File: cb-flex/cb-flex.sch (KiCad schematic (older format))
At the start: 26 parts, among them P3 CONN_01X01, SW1 SW_PUSH_SMALL, U1 SI7021, U4 ANTENNA

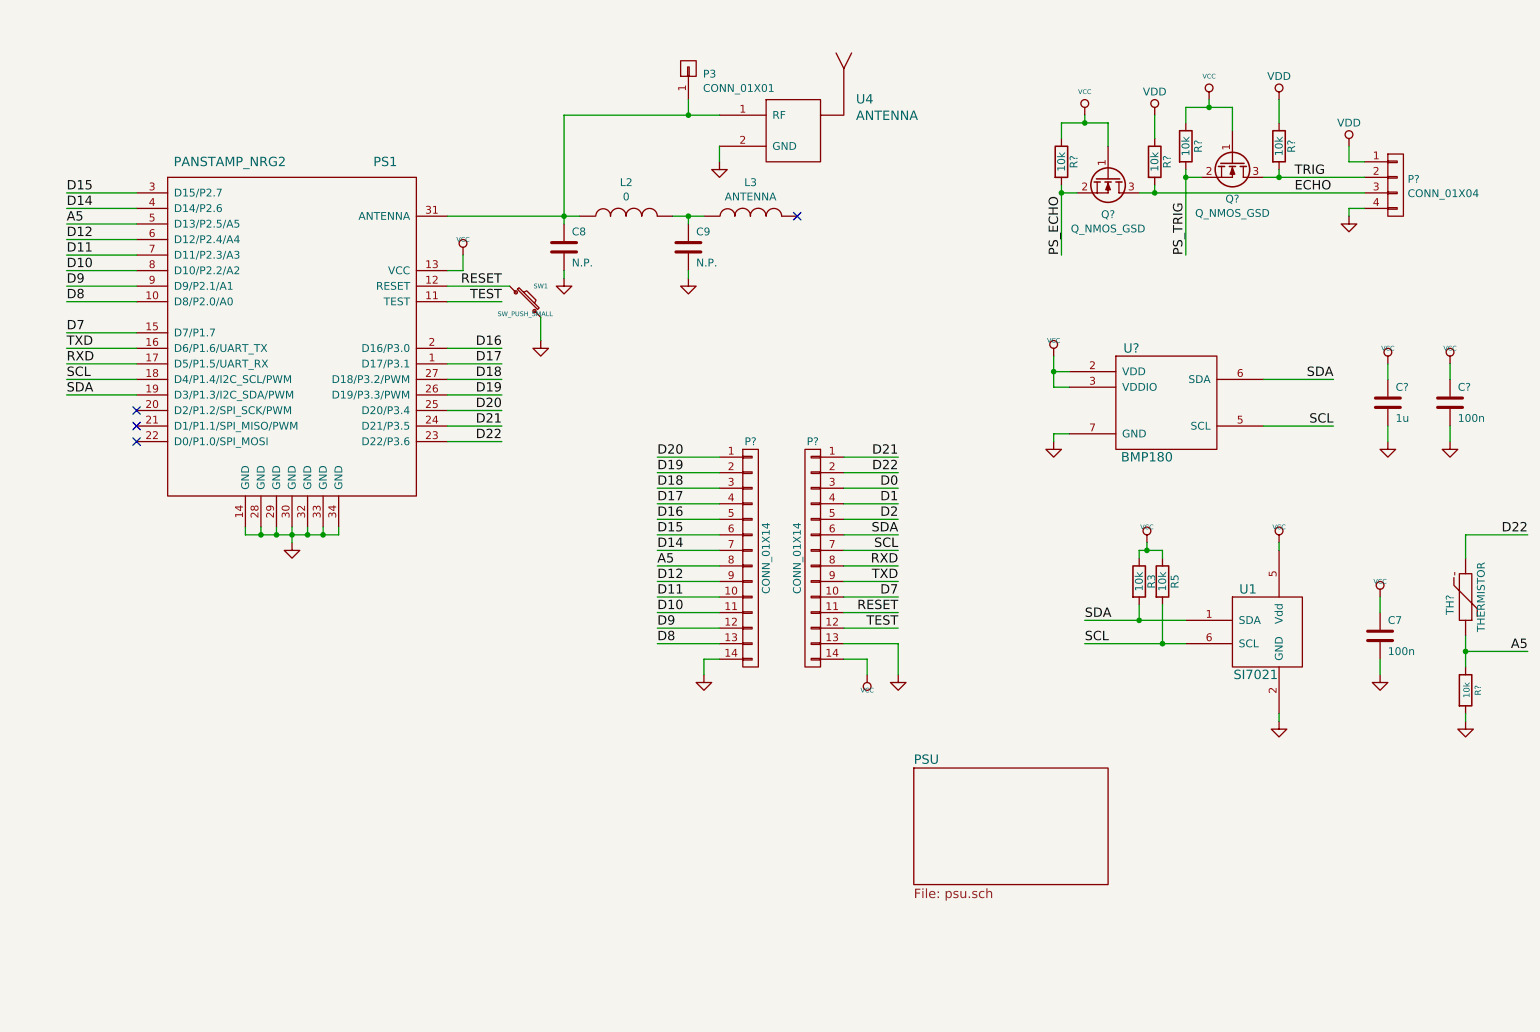
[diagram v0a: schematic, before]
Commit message: Finishing schematic and starting PCB layout
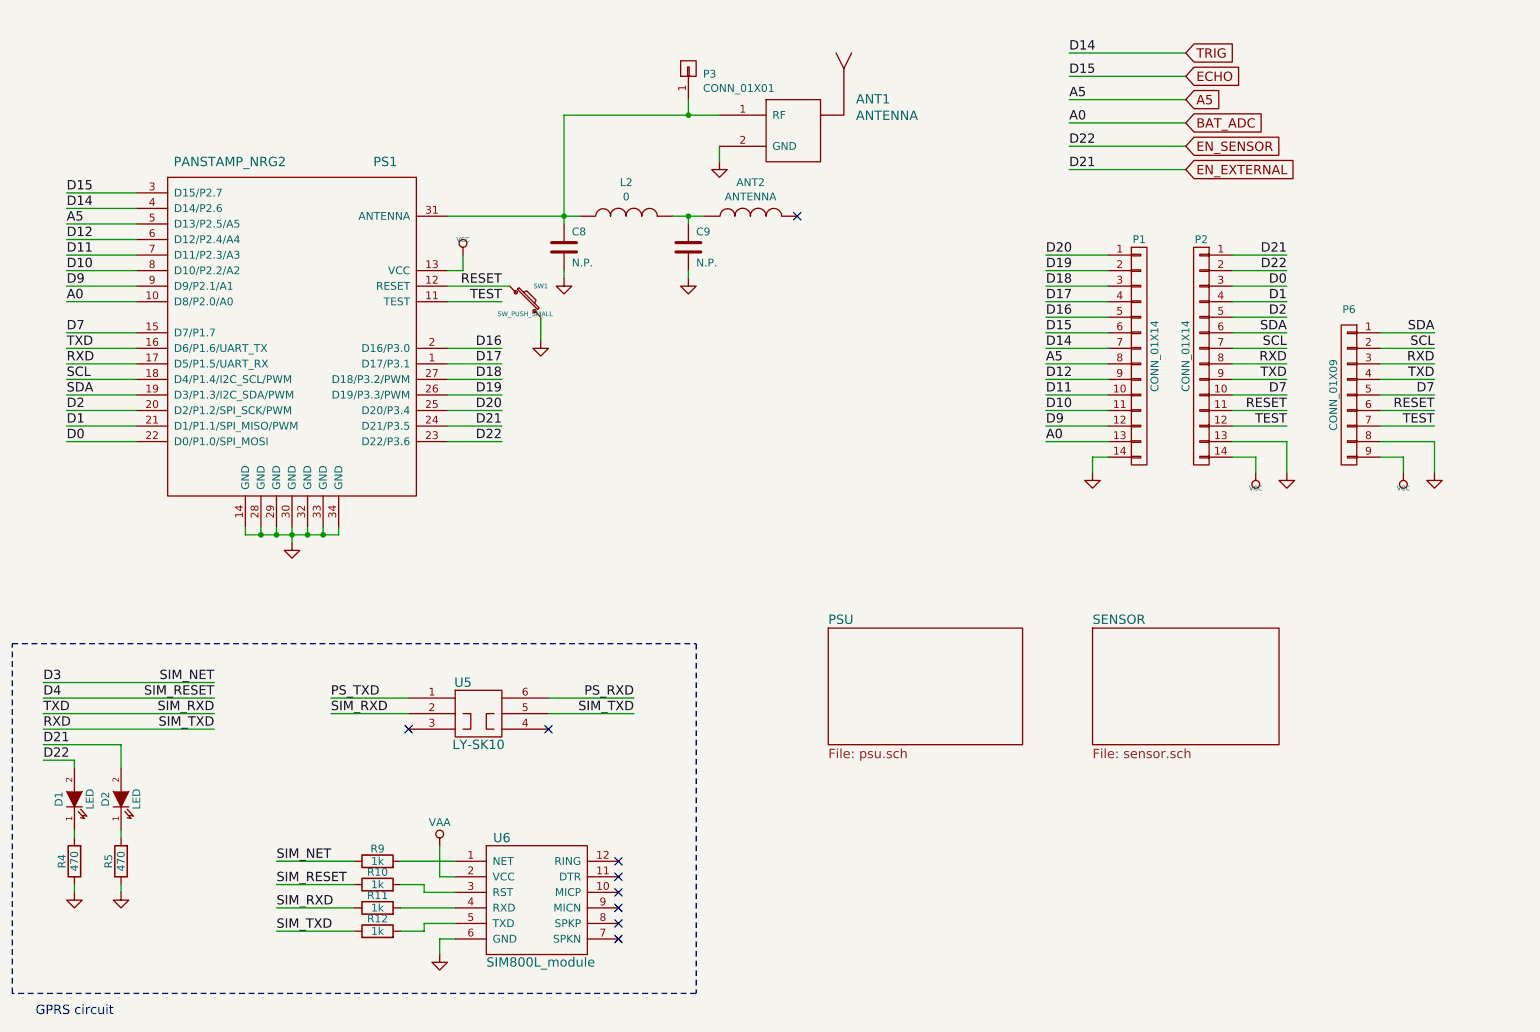
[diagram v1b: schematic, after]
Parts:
- removed C7, C?: 100n, mysmd:SM0603S, symbol C
- removed C?: 1u, mysmd:SM0603S, symbol C
- removed P?: CONN_01X04, symbol CONN_01X04
- removed Q? (x2): Q_NMOS_GSD, mysmd:SOT23, symbol Q_NMOS_GSD
- removed R3, R? (x5): 10k, mysmd:SM0603S, symbol R
- removed TH?: THERMISTOR, mysmd:SM0603S, symbol THERMISTOR
- removed U1: SI7021, mysmd:DFN-6, symbol SI7021
- removed U?: BMP180, mysmd:BMP180, symbol BMP180
- added D1, D2: LED, mysmd:SM0603S_POL, symbol LED
- added P6: CONN_01X09, Pin_Headers:Pin_Header_Straight_1x09, symbol CONN_01X09
- added R10, R11, R12, R9: 1k, mysmd:SM0603S, symbol R
- added R4: 470, mysmd:SM0603S, symbol R
- added U5: LY-SK10, mysmd:LY-SK10, symbol LY-SK10
- added U6: SIM800L_module, mymods:SIM800L_MODULE, symbol SIM800L_module
- R5: value 10k -> 470
- gave numbers to parts that had none: 2
- renumbered U4 to ANT1, L3 to ANT2
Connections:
- net D14 is gone; now on net TRIG: P1.7 (P7), PS1.4 (D14/P2.6)
- net D15 is gone; now on net ECHO: P1.6 (P6), PS1.3 (D15/P2.7)
- net D0: now also PS1.22 (D0/P1.0/SPI_MOSI)
- net D1: now also PS1.21 (D1/P1.1/SPI_MISO/PWM)
- net D2: now also PS1.20 (D2/P1.2/SPI_SCK/PWM)
- net D7: now also P6.5 (P5)
- net GND: now also R5.1, P6.8 (P8), R4.1, U6.6 (GND)
- net RESET: now also P6.6 (P6)
- net RXD: now also P6.3 (P3), R12.1, U5.5
- net SCL: now also P6.2 (P2); no longer R5.2
- net SDA: now also P6.1 (P1)
- net TEST: now also P6.7 (P7)
- net VCC: now also P6.9 (P9); no longer R5.1
- net D21 renamed EN_EXTERNAL
- net EN_EXTERNAL: now also D2.2 (A)
- net D22 renamed EN_SENSOR
- net EN_SENSOR: now also D1.2 (A)
- net D8 renamed BAT_ADC
- net TXD renamed SIM_RXD
- net SIM_RXD: now also P6.4 (P4), R11.1, U5.2
- new net: D2.1 (K), R5.2
- new net: R9.2, U6.1 (NET)
- new net: R10.2, U6.3 (RST)
- new net: R11.2, U6.4 (RXD)
- new net: R12.2, U6.5 (TXD)
- new net: D1.1 (K), R4.2
- new net D3: R9.1
- new net D4: R10.1
- new net PS_RXD: U5.6
- new net PS_TXD: U5.1
- new net VAA: U6.2 (VCC)
- no-connect marks 4 -> 9
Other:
- note added: "GPRS circuit"
- moved on the sheet: P1, P2

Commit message: Finishing layout
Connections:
- net D16 is gone; now on net EN_EXTERNAL: P1.5 (P5), PS1.2 (D16/P3.0)
- net D20 is gone; now on net EN_SENSOR: P1.1 (P1), PS1.25 (D20/P3.4)
- net D3 is gone; now on net ACC_INT1: R9.1
- net D4 is gone; now on net ACC_INT2: R10.1
- net PS_RXD is gone; now on net RXD: U5.6
- net EN_EXTERNAL: no longer D2.2 (A), P2.1 (P1), PS1.24 (D21/P3.5)
- net EN_SENSOR: no longer D1.2 (A), P2.2 (P2), PS1.23 (D22/P3.6)
- net RXD: no longer R12.1, U5.5
- net SIM_RXD: no longer P2.9 (P9), P6.4 (P4), PS1.16 (D6/P1.6/UART_TX)
- net BAT_ADC renamed +BATT
- net D0 renamed EN_ACC
- net D1 renamed ACC_INT1
- net D2 renamed ACC_INT2
- net PS_TXD renamed TXD
- net TXD: now also P2.9 (P9), P6.4 (P4), PS1.16 (D6/P1.6/UART_TX)
- new net D21: D2.2 (A), P2.1 (P1), PS1.24 (D21/P3.5)
- new net D22: D1.2 (A), P2.2 (P2), PS1.23 (D22/P3.6)
- new net SIM_TXD: R12.1, U5.5
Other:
- moved on the sheet: P1, P2, P6

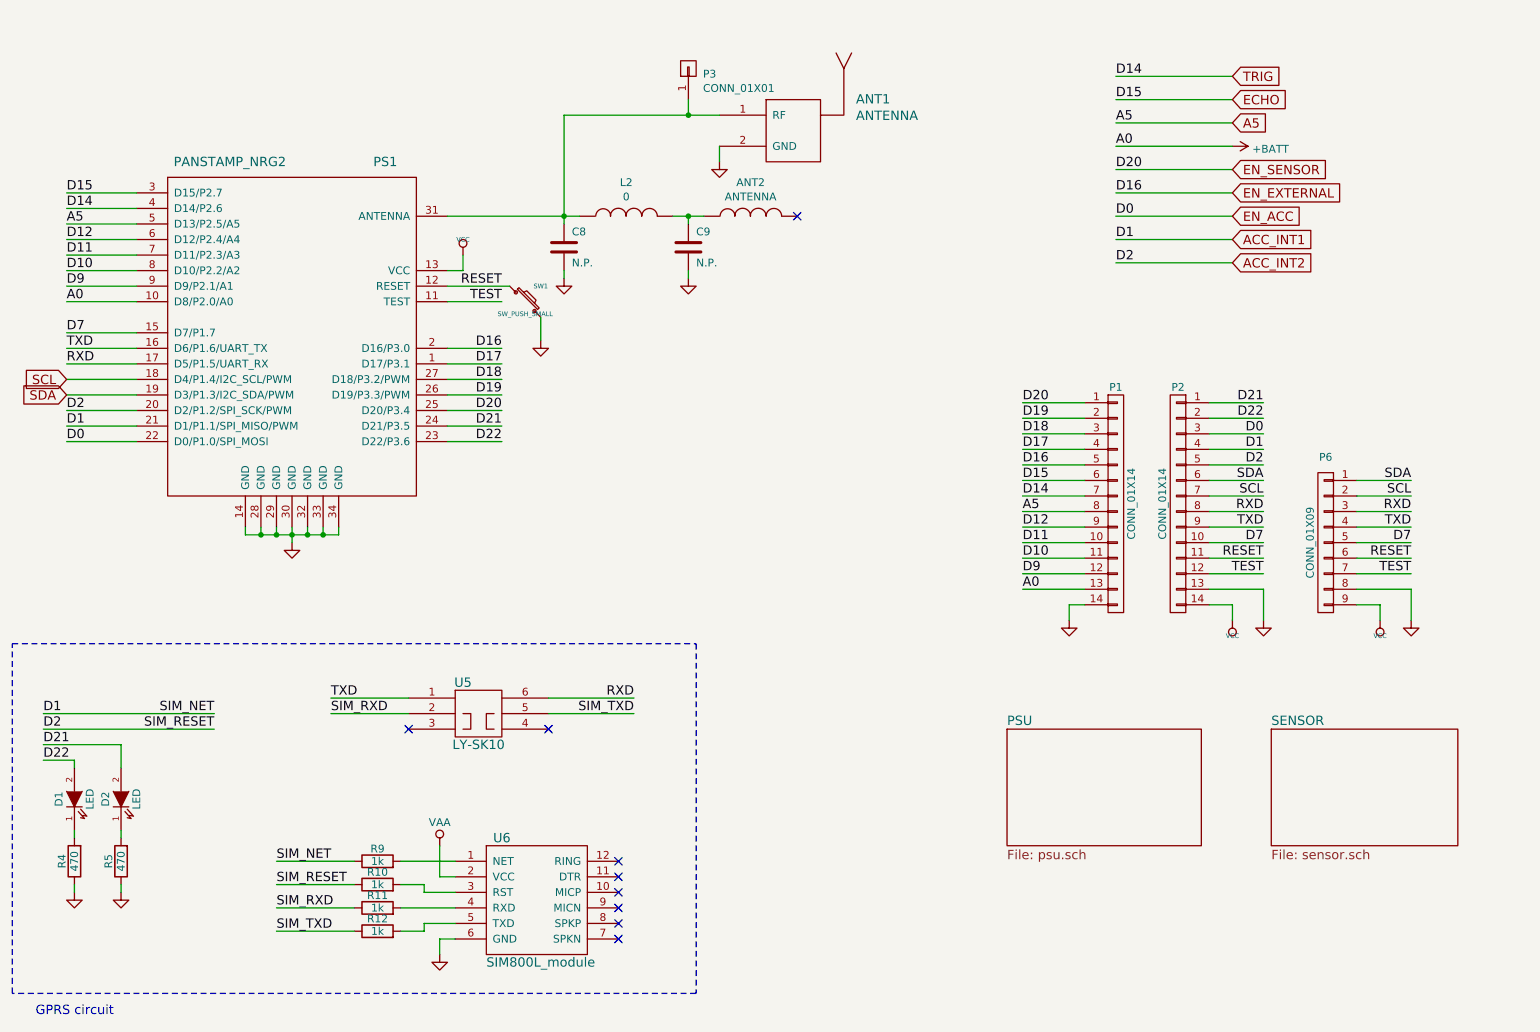
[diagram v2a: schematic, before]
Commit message: PCB layour finished
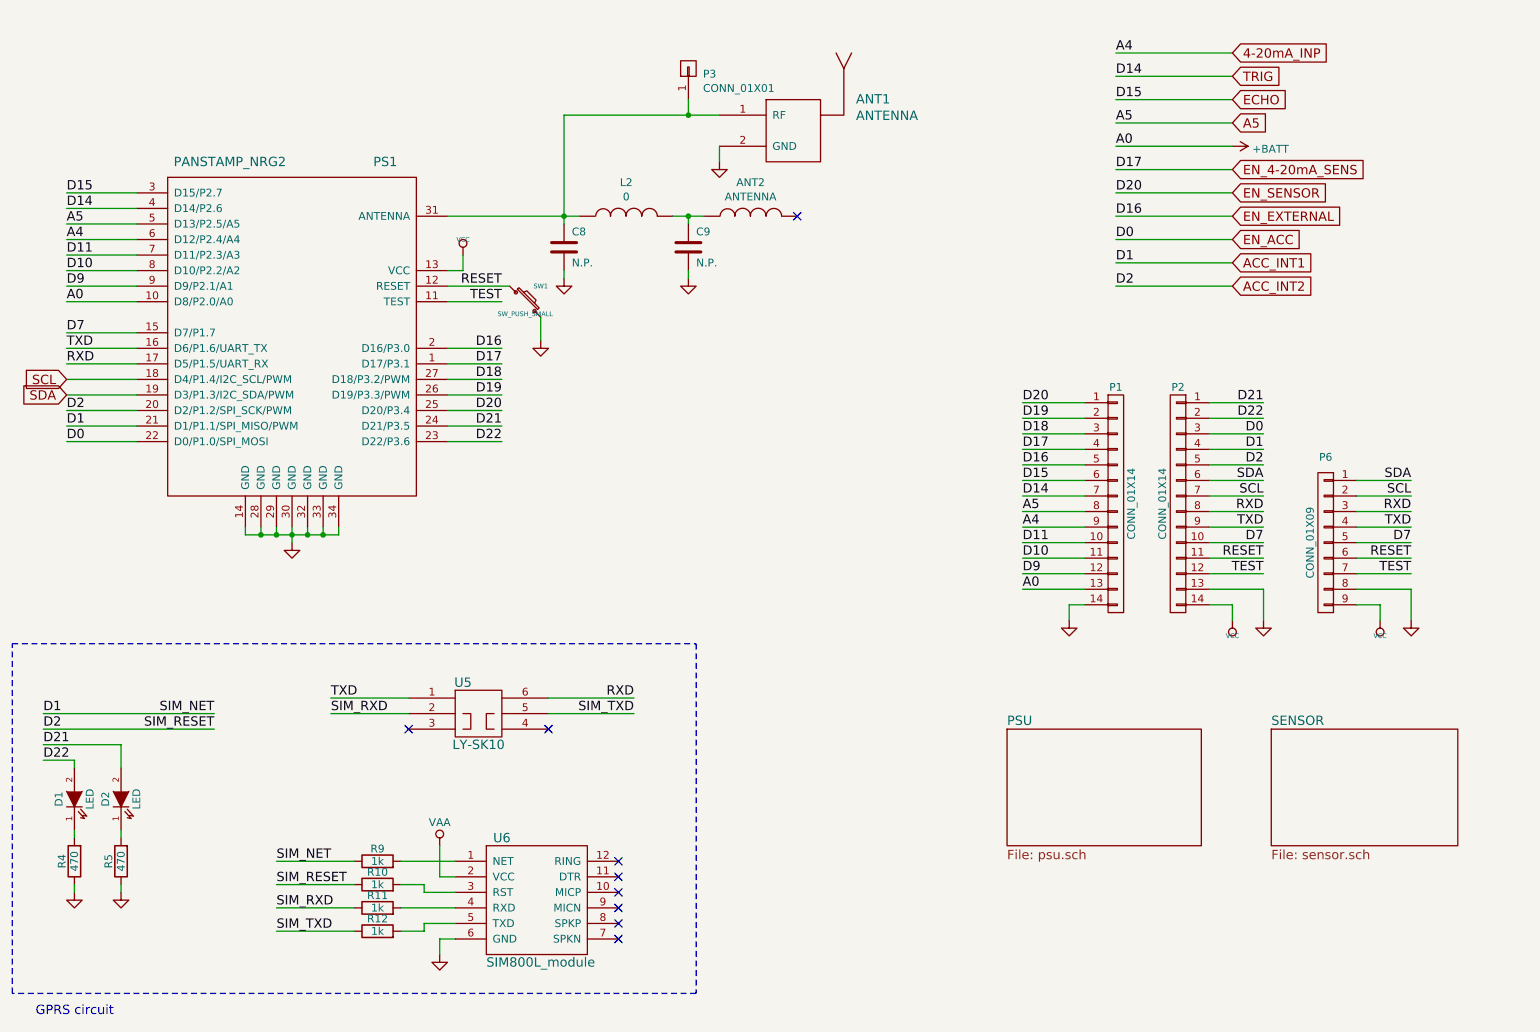
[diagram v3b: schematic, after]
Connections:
- net D12 renamed 4-20mA_INP
- net D17 renamed EN_4-20mA_SENS
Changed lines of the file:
@@
 D11
 Text Label 1500 2100 0    60   ~ 0
-D12
+A4
 Text Label 1500 1900 0    60   ~ 0
 D14
@@
 A5
 Text Label 7650 3950 0    60   ~ 0
-D12
+A4
 Text Label 7650 4050 0    60   ~ 0
 D11
@@
 Text Label 1500 2000 0    60   ~ 0
 A5
-Text GLabel 9000 1650 2    60   Input ~ 0
+Text GLabel 9000 1800 2    60   Input ~ 0
 EN_SENSOR
 Wire Wire Line
-	9000 1650 8250 1650
-Text Label 8250 1650 0    60   ~ 0
+	9000 1800 8250 1800
+Text Label 8250 1800 0    60   ~ 0
 D20
 Text GLabel 9000 1350 2    60   Input ~ 0
@@
 Text Label 8250 1200 0    60   ~ 0
 D15
-Text GLabel 9000 1800 2    60   Input ~ 0
+Text GLabel 9000 1950 2    60   Input ~ 0
 EN_EXTERNAL
 Wire Wire Line
-	9000 1800 8250 1800
-Text Label 8250 1800 0    60   ~ 0
+	9000 1950 8250 1950
+Text Label 8250 1950 0    60   ~ 0
 D16
 $Comp
@@
 Text Label 8250 1500 0    60   ~ 0
 A0
+Text GLabel 9000 2250 2    60   Input ~ 0
+ACC_INT1
+Wire Wire Line
+	9000 2250 8250 2250
+Text Label 8250 2250 0    60   ~ 0
+D1
+Text GLabel 9000 2400 2    60   Input ~ 0
+ACC_INT2
+Wire Wire Line
+	9000 2400 8250 2400
+Text Label 8250 2400 0    60   ~ 0
+D2
 Text GLabel 9000 2100 2    60   Input ~ 0
-ACC_INT1
+EN_ACC
 Wire Wire Line
 	9000 2100 8250 2100
 Text Label 8250 2100 0    60   ~ 0
-D1
-Text GLabel 9000 2250 2    60   Input ~ 0
-ACC_INT2
-Wire Wire Line
-	9000 2250 8250 2250
-Text Label 8250 2250 0    60   ~ 0
-D2
-Text GLabel 9000 1950 2    60   Input ~ 0
-EN_ACC
-Wire Wire Line
-	9000 1950 8250 1950
-Text Label 8250 1950 0    60   ~ 0
 D0
 Text GLabel 1500 3000 0    60   Input ~ 0
@@
 SDA
 $Comp
-L +BATT #PWR?
+L +BATT #PWR016
 U 1 1 56C22796
 P 9000 1500
-F 0 "#PWR?" H 9000 1350 50  0001 C CNN
+F 0 "#PWR016" H 9000 1350 50  0001 C CNN
 F 1 "+BATT" V 9018 1628 50  0000 L CNN
 F 2 "" H 9000 1500 50  0000 C CNN
@@
 	0    1    1    0
 $EndComp
+Text Label 8250 900  0    60   ~ 0
+A4
+Text GLabel 9000 900  2    60   Input ~ 0
+4-20mA_INP
+Wire Wire Line
+	9000 900  8250 900
+Text GLabel 9000 1650 2    60   Input ~ 0
+EN_4-20mA_SENS
+Wire Wire Line
+	9000 1650 8250 1650
+Text Label 8250 1650 0    60   ~ 0
+D17
 $EndSCHEMATC

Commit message: PCB layout finished
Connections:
- net D11 is gone; now on net 4-20mA_INP: P1.10 (P10), PS1.7 (D11/P2.3/A3)
- net 4-20mA_INP: no longer P1.9 (P9), PS1.6 (D12/P2.4/A4)
- new net VEXT: P1.9 (P9), PS1.6 (D12/P2.4/A4)
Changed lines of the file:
@@
 D10
 Text Label 1500 2200 0    60   ~ 0
-D11
+A3
 Text Label 1500 2100 0    60   ~ 0
 A4
@@
 A4
 Text Label 7650 4050 0    60   ~ 0
-D11
+A3
 Text Label 7650 4150 0    60   ~ 0
 D10
@@
 	0    1    1    0
 $EndComp
-Text Label 8250 900  0    60   ~ 0
+Text Label 8250 750  0    60   ~ 0
 A4
 Text GLabel 9000 900  2    60   Input ~ 0
@@
 Text Label 8250 1650 0    60   ~ 0
 D17
+Text Label 8250 900  0    60   ~ 0
+A3
+Text GLabel 9000 750  2    60   Input ~ 0
+VEXT
+Wire Wire Line
+	9000 750  8250 750
 $EndSCHEMATC
